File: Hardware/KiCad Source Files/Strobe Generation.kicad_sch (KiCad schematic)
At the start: 23 parts, among them Q1 IRLU024NPBF, Q2 IRLU024NPBF, Q3 Q_NMOS

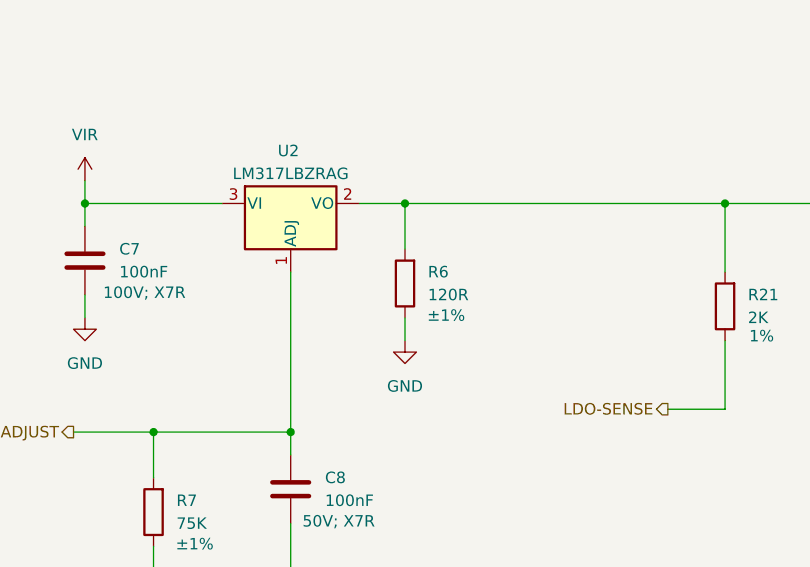
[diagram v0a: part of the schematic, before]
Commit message: Remove R6 from BOM and Centroid files.
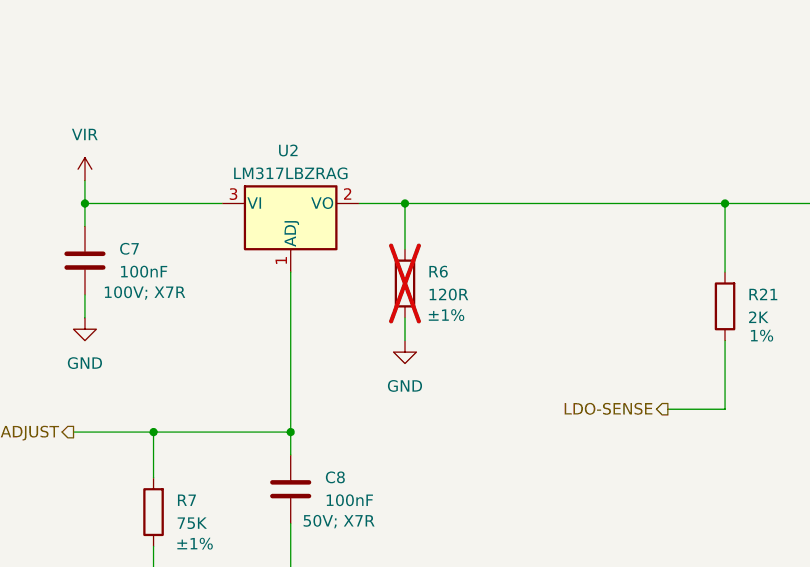
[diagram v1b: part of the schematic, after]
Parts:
- R6: now not fitted
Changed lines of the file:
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@@
 		(in_bom yes)
 		(on_board yes)
-		(dnp no)
+		(dnp yes)
 		(property "Reference" "R6"
 			(at 83.82 58.4199 0)

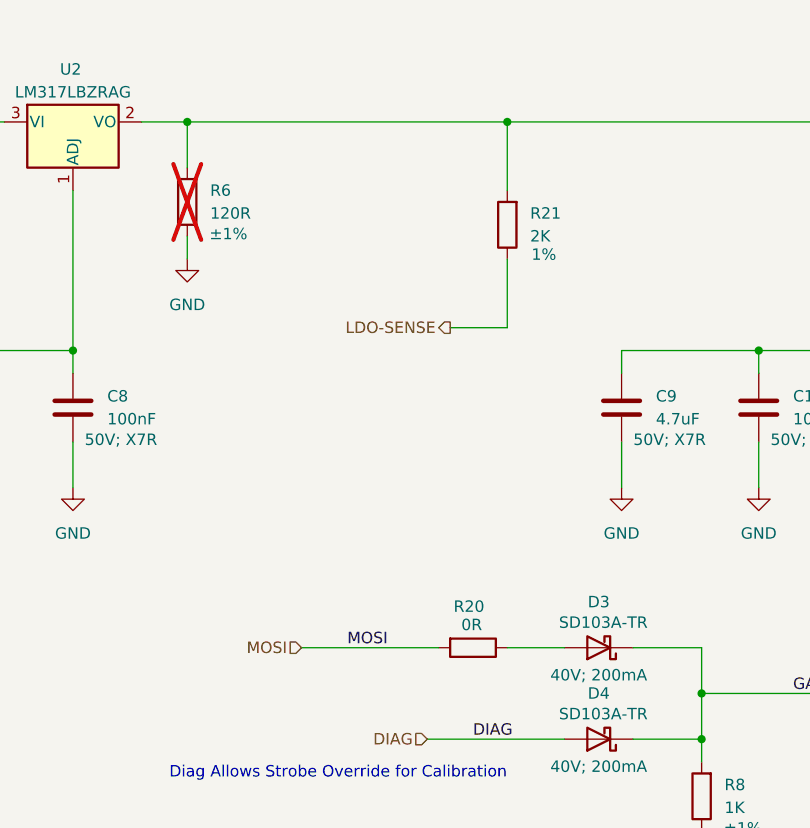
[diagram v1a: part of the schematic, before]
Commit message: Finalized V3 Connector BOM based on testing on hardware.
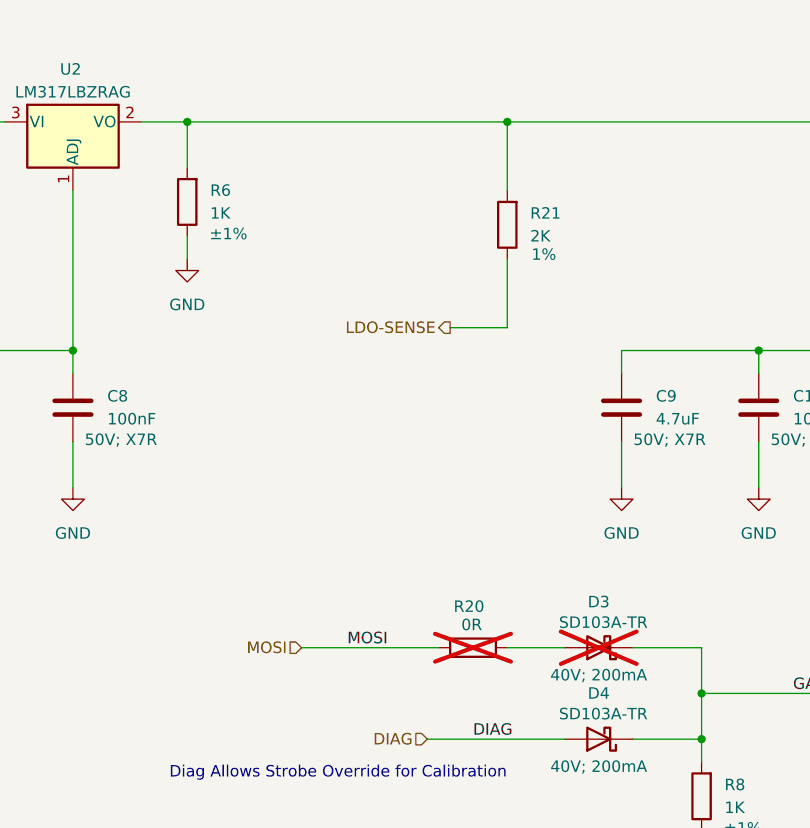
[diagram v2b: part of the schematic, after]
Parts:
- D3, R20: now not fitted
- R6: value 120R -> 1K; Part Number MFR-25FTE52-120R -> MFR-25FRF52-1K; now fitted
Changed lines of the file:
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@@
 		(in_bom yes)
 		(on_board yes)
-		(dnp no)
+		(dnp yes)
 		(property "Reference" "D3"
 			(at 127 104.14 0)
@@
 		(in_bom yes)
 		(on_board yes)
-		(dnp yes)
+		(dnp no)
 		(property "Reference" "R6"
 			(at 83.82 58.4199 0)
@@
 			)
 		)
-		(property "Value" "120R"
+		(property "Value" "1K"
 			(at 83.82 60.9599 0)
 			(effects
@@
 			)
 		)
-		(property "Part Number" "MFR-25FTE52-120R"
+		(property "Part Number" "MFR-25FRF52-1K"
 			(at 81.28 59.69 90)
 			(effects
@@
 		(in_bom yes)
 		(on_board yes)
-		(dnp no)
+		(dnp yes)
 		(property "Reference" "R20"
 			(at 114.3 104.648 90)
